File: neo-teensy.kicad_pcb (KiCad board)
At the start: 2 copper layers, 30.5 x 38.1 mm, 32 parts, among them J1 Conn_01x03_Male, J10 Conn_01x14, J11 Conn_02x04_Odd_Even, J12 Conn_01x02, J2 Conn_01x03_Male, J3 Conn_01x14_Male, J4 Conn_01x03_Male, J5 Conn_01x05_Male, J6 Conn_01x03_Male, J7 Conn_01x14_Male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

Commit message: Minor silk-screen fix.
Signed-off-by: Aaron Williams <aaron.w2@gmail.com>
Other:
- board text added: "Neo Teensy"
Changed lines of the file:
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@@
   (general
     (thickness 1.6)
-    (drawings 39)
+    (drawings 40)
     (tracks 545)
     (zones 0)
@@
     )
   )
+  (gr_text "Neo Teensy" (at 35.3949 45.0723 90) (layer B.SilkS)
+    (effects (font (size 1.5 1.5) (thickness 0.15)) (justify mirror))
+  )
   (gr_line (start 27.7368 38.7604) (end 27.7876 38.2016) (layer B.SilkS) (width 0.12))
   (gr_text DO (at 23.7744 67.564 90) (layer F.SilkS)
@@
     (effects (font (size 1 1) (thickness 0.15)) (justify mirror))
   )
-  (gr_text "NeoPixel Driver Board\n© 2019 by Aaron Williams\nDesigned for Teensy 3.2 and 4.0" (at 30.7721 45.847 90) (layer B.SilkS)
+  (gr_text "NeoPixel Driver Board\n© 2019 by Aaron Williams\nDesigned for Teensy 3.2 and 4.0" (at 30.2895 49.022 90) (layer B.SilkS)
     (effects (font (size 1 1) (thickness 0.15)) (justify mirror))
   )

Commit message: Minor cleanup.
Signed-off-by: Aaron Williams <aaron.w2@gmail.com>
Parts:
- moved J10 0.05 mm to (21.6, 67.6)
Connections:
- J10 pad 1: /DO_R -> /DO
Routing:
- net GND: track 139.6 -> 177.2 mm, vias 49 -> 53
- net /DO: track 6.82 -> 34.1 mm
- net /IO0: track 8.57 -> 7.89 mm
- net (no net): vias 1 -> 0

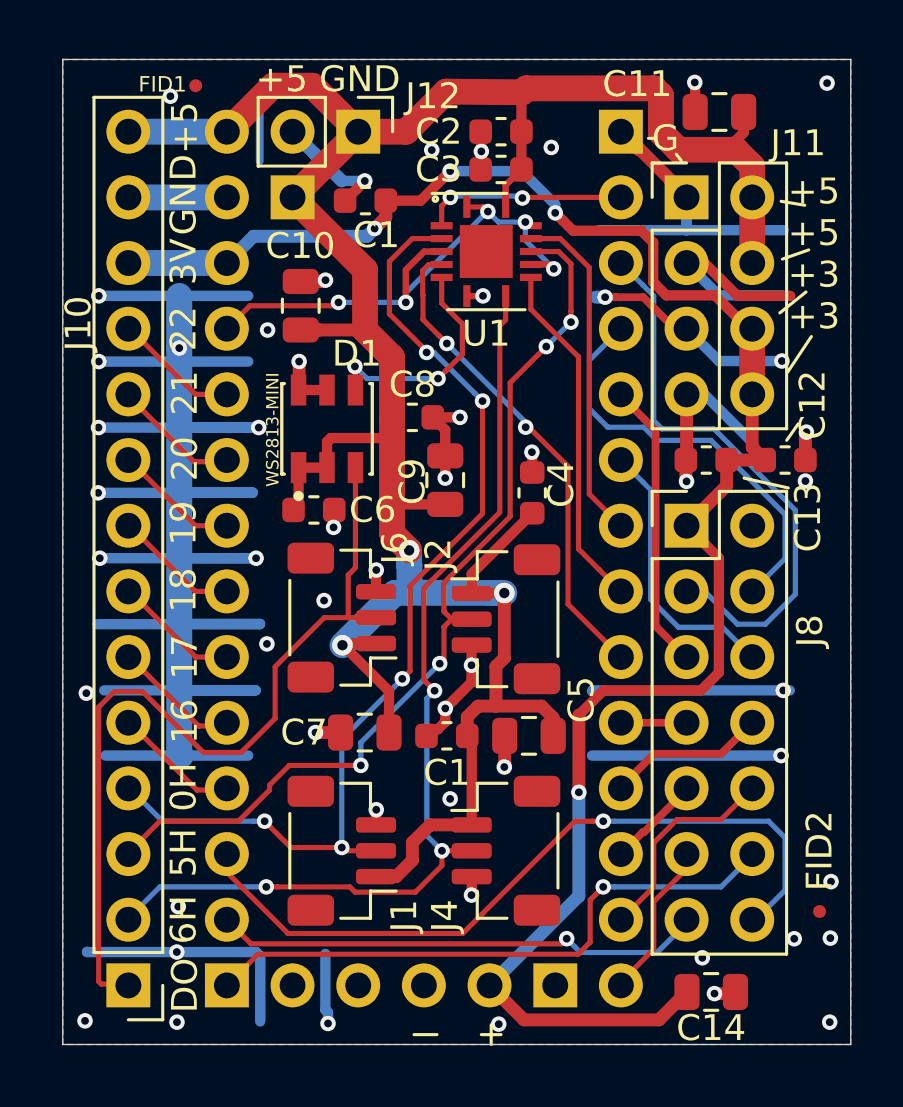
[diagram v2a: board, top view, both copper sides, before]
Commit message: Removed connectors and added 12V boost
Version 3.1.0

Signed-off-by: Aaron Williams <aaron.w2@gmail.com>
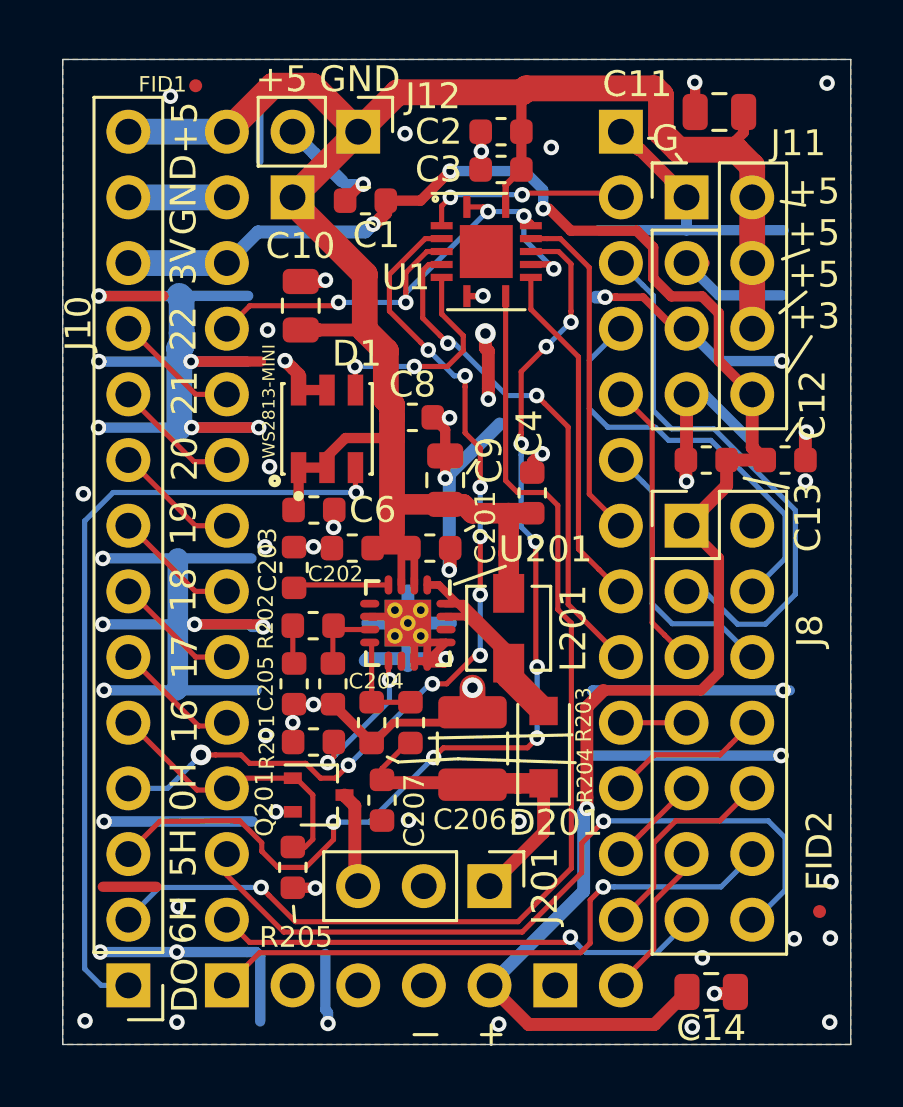
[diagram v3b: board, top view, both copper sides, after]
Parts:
- removed the C1 at (33.9, 57.9)
- removed C5, C7: 10uF, Capacitor_SMD:C_0805_2012Metric
- removed J1, J2, J4, J6: Conn_01x03_Male, Connector_JST:JST_SH_BM03B-SRSS-TB_1x03-1MP_P1.00mm_Vertical
- added C201: 6.8uF, Capacitor_SMD:C_0603_1608Metric, F.Cu at (33.2, 50.6)
- added C202: 100nF, Capacitor_SMD:C_0603_1608Metric, F.Cu at (30.2, 50.6)
- added C203: 22nF, Capacitor_SMD:C_0603_1608Metric, F.Cu at (28.0, 51.4)
- added C204: 820pF, Capacitor_SMD:C_0603_1608Metric, F.Cu at (29.5, 55.9)
- added C205: 47nF, Capacitor_SMD:C_0603_1608Metric, F.Cu at (28.0, 55.9)
- added C206: 22uF, Capacitor_SMD:C_1210_3225Metric, F.Cu at (34.9, 58.4)
- added C207: 1uF, Capacitor_SMD:C_0603_1608Metric, F.Cu at (31.4, 60.4)
- added D201: SS24FL, Diode_SMD:D_SOD-123F, F.Cu at (37.6, 58.4)
- added J201: Conn_01x03, Connector_PinHeader_2.54mm:PinHeader_1x03_P2.54mm_Vertical, F.Cu at (35.6, 63.7)
- added L201: 3.3uH, Aaron:L_Vishay_IHLP-1212, F.Cu at (36.3, 53.8)
- added Q201: BSS214NW, Package_TO_SOT_SMD:SOT-323_SC-70, F.Cu at (28.9, 60.2)
- added R201: 18.2k, Resistor_SMD:R_0603_1608Metric, F.Cu at (28.8, 58.1)
- added R202: 1.69k, Resistor_SMD:R_0603_1608Metric, F.Cu at (28.7, 53.6)
- added R203: 86.6k, Resistor_SMD:R_0603_1608Metric, F.Cu at (32.5, 57.4)
- added R204: 10k, Resistor_SMD:R_0603_1608Metric, F.Cu at (31.0, 57.4)
- added R205: 100k, Resistor_SMD:R_0603_1608Metric, F.Cu at (27.9, 63.0)
- added U201: TPS55340-Q1, Aaron:QFN-16-1EP_3x3mm_P0.5mm_EP2.7x2.7mm_ThermalVias, F.Cu at (32.4, 53.5)
- moved REF** 2.78 mm to (36.1, 56.2)
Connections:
- net /IO16 renamed FET_CTL
- J11 pad 6: +3V3 -> +5V
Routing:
- net +5V: track 106.6 -> 82.4 mm, vias 3 -> 0
- net /12-Boost/SW: track 0.00 -> 13.8 mm
- net +12V: track 0.00 -> 13.1 mm
- net GND: track 177.2 -> 186.7 mm, vias 53 -> 64
- net FET_CTL: track 4.94 -> 11.3 mm
- net /12-Boost/FREQ: track 0.00 -> 5.83 mm, vias 0 -> 2
- net /IO5_H: track 36.0 -> 41.0 mm, vias 4 -> 8
- net /IO6_H: track 38.2 -> 42.8 mm, vias 3 -> 1
- net /IO0_H: track 39.6 -> 35.5 mm, vias 5 -> 9
- net /12-Boost/FB: track 0.00 -> 3.84 mm
- net /12-Boost/FET_DRV: track 0.00 -> 3.74 mm
- net /12-Boost/SS: track 0.00 -> 3.70 mm
- net /12-Boost/COMP: track 0.00 -> 2.93 mm
- net /DO: track 34.1 -> 31.2 mm, vias 0 -> 1
- net Net-(C205-Pad1): track 0.00 -> 1.48 mm
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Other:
- board text added: "+5 +5 +5 +3"
- board text added: "Revision 3.1"
- board text removed: "+5 +5 +3 +3"
- board text removed: "Revision 3.0"

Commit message: Fixed GPIO 13, GPIO 16 and GPIO 17 for the fan control.
Signed-off-by: Aaron Williams <aaron.w2@gmail.com>
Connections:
- J10 pad 5: FET_CTL -> /IO13
- J10 pad 6: /IO17 -> FET_CTL
- J7 pad 4: FET_CTL -> /IO16
- J7 pad 5: /IO17 -> FET_CTL
- J8 pad 12: /IO13 -> /IO14
- J8 pad 13: /IO14 -> /IO15
- J8 pad 14: /IO15 -> /IO16
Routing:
- net GND: track 186.7 -> 245.8 mm, vias 64 -> 69
- net /IO16: track 0.00 -> 32.0 mm, vias 0 -> 1
- net /IO15: track 29.9 -> 20.6 mm, vias 1 -> 0
- net /IO13: track 23.5 -> 14.8 mm, vias 1 -> 0
- net /IO17: track 4.81 -> 0.00 mm
- net /IO14: track 19.0 -> 23.4 mm, vias 1 -> 0
- net /IO20: track 4.91 -> 6.07 mm
- net FET_CTL: track 11.3 -> 12.3 mm
- net /IO6_H: track 42.8 -> 42.6 mm, vias 1 -> 2
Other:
- rule trace_min: 0.2 -> 0.1524
- rule via_min_drill: 0.3 -> 0.254
- rule via_min_size: 0.4 -> 0.508
- board text added: "13"
- board text added: "GND +5"
- board text added: "Revision 3.1.1"
- board text removed: "+5 GND"
- board text removed: "16"
- board text removed: "Revision 3.1"

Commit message: Minor fixups, changed solder mask.
Signed-off-by: Aaron Williams <aaron.w2@gmail.com>
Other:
- rule pad_to_mask_clearance: 0.051 -> 0.0508
- rule solder_mask_min_width: 0.25 -> 0.101
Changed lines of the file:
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@@
   )
   (setup
-    (last_trace_width 0.8)
+    (last_trace_width 0.25)
     (user_trace_width 0.1524)
     (user_trace_width 0.2)
@@
     (pad_size 1.7 1.7)
     (pad_drill 1)
-    (pad_to_mask_clearance 0.051)
-    (solder_mask_min_width 0.25)
+    (pad_to_mask_clearance 0.0508)
+    (solder_mask_min_width 0.101)
     (aux_axis_origin 0 0)
     (visible_elements FFFFFF7F)

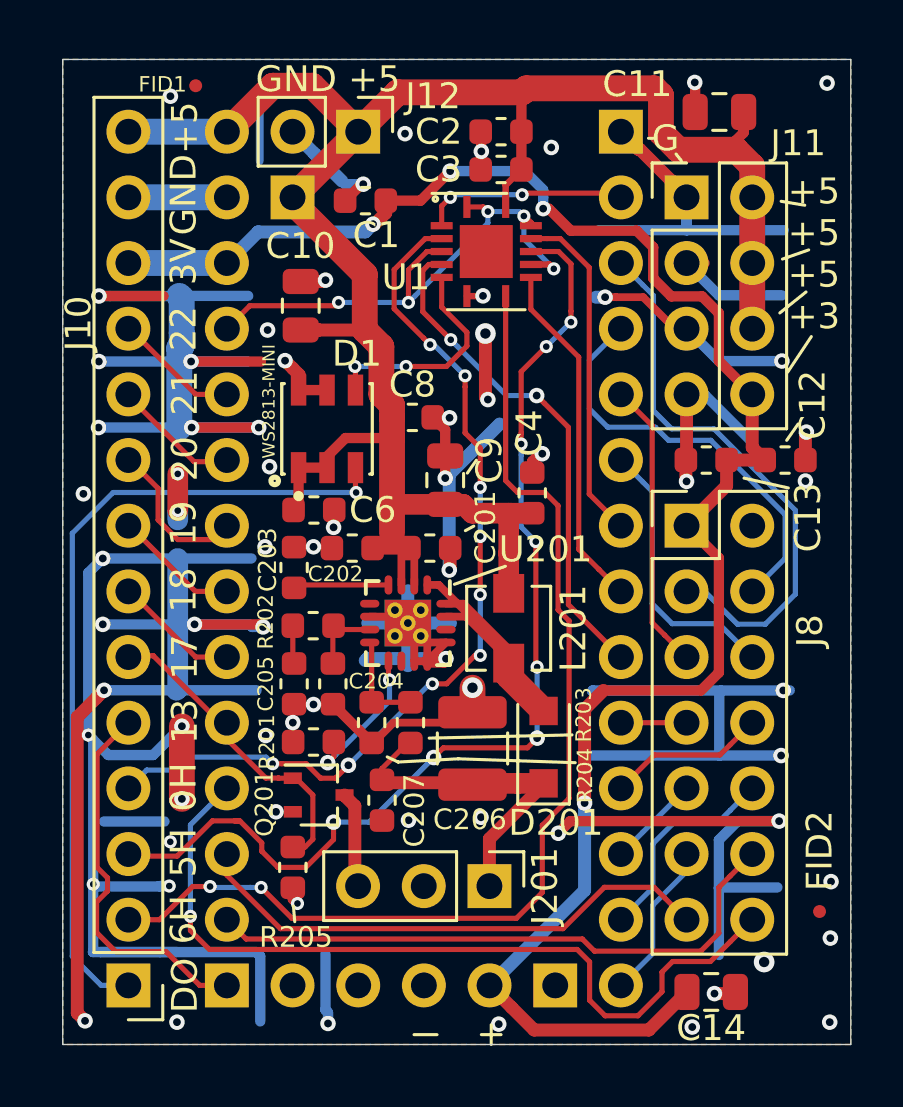
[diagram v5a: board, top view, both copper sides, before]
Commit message: Changed GPIOs for Teensy 4.0
The 5V GPIOs were changed for the Teensy 4.0.  In addition the GPIOs to
the 14 pin header were also changed.

Some component values were also changed for the power supply.

Note that this is still compatible with the 3.1 stencil.

This also fixes the 12V BOM.

Signed-off-by: Aaron Williams <aaron.w2@gmail.com>
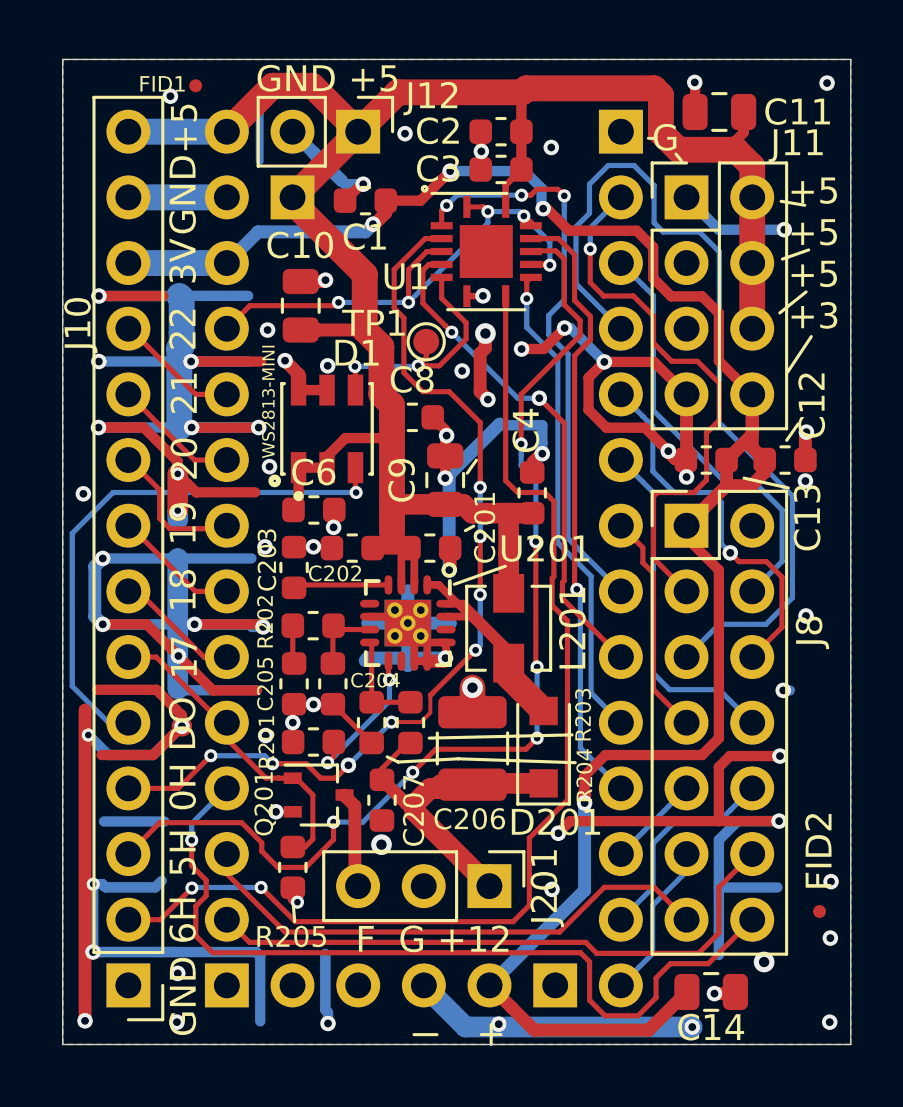
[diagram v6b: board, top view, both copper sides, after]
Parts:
- added TP1: TestPoint, TestPoint:TestPoint_Pad_D1.0mm, F.Cu at (33.1, 42.7)
- C201: value 6.8uF -> 22uF
- C202: value 100nF -> 0.1uF
- C206: value 22uF -> 47uF
- C6: value 0.1uF -> 1uF
- R201: value 18.2k -> 18.7K
- R202: value 1.69k -> 1.62k
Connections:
- net /IO5_H renamed /IO9_H
- J10 pad 1: /DO -> GND
- J10 pad 2: /IO6_H -> /IO8_H
- J10 pad 4: /IO0_H -> /IO6_H
- J10 pad 5: /IO13 -> /DO
- J8 pad 3: /IO1 -> /IO0
- J8 pad 4: /IO2 -> /IO1
- J8 pad 5: /IO3 -> /IO2
- J8 pad 6: /IO4 -> /IO3
- J8 pad 7: /IO8 -> /IO5
- J8 pad 8: /IO9 -> /IO4
- U1 pad 12: /IO5 -> /IO9
- U1 pad 2: /IO0 -> /IO6
- U1 pad 3: /IO0_H -> /IO6_H
- U1 pad 8: /IO6_H -> /IO8_H
- U1 pad 9: /IO6 -> /IO8
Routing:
- net /IO8_H: track 0.00 -> 42.7 mm, vias 0 -> 2
- net /IO0_H: track 35.1 -> 0.00 mm, vias 9 -> 0
- net /IO9: track 6.13 -> 23.8 mm, vias 0 -> 1
- net /IO2: track 16.4 -> 33.7 mm
- net /IO8: track 2.54 -> 18.8 mm, vias 0 -> 1
- net /IO13: track 14.8 -> 0.00 mm
- net /IO0: track 7.97 -> 21.5 mm, vias 2 -> 1
- net /DO: track 31.6 -> 21.3 mm
- net GND: track 245.8 -> 236.6 mm, vias 69 -> 74
- net /IO6: track 13.6 -> 22.5 mm, vias 0 -> 3
- net /IO6_H: track 42.6 -> 35.9 mm, vias 2 -> 8
- net /IO1: track 21.8 -> 16.4 mm
- net /IO5: track 13.2 -> 8.67 mm
- net +3V3: track 72.2 -> 75.8 mm
- net /IO3: track 11.2 -> 14.7 mm, vias 0 -> 1
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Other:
- board text added: "F G +12"
- board text added: "NeoPixel Driver Board © 2019 by Aaron Williams Designed for Teensy 4.0 and 3.2"
- board text added: "Revision 3.2.0"
- board text added: "U201:"
- board text removed: "13"
- board text removed: "NeoPixel Driver Board © 2019 by Aaron Williams Designed for Teensy 3.2 and 4.0"
- board text removed: "Revision 3.1.1"

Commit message: Added pull-up resistors to 14-pin header
Made board 4 layers

Made board double sided

Signed-off-by: Aaron Williams <aaron.w2@gmail.com>
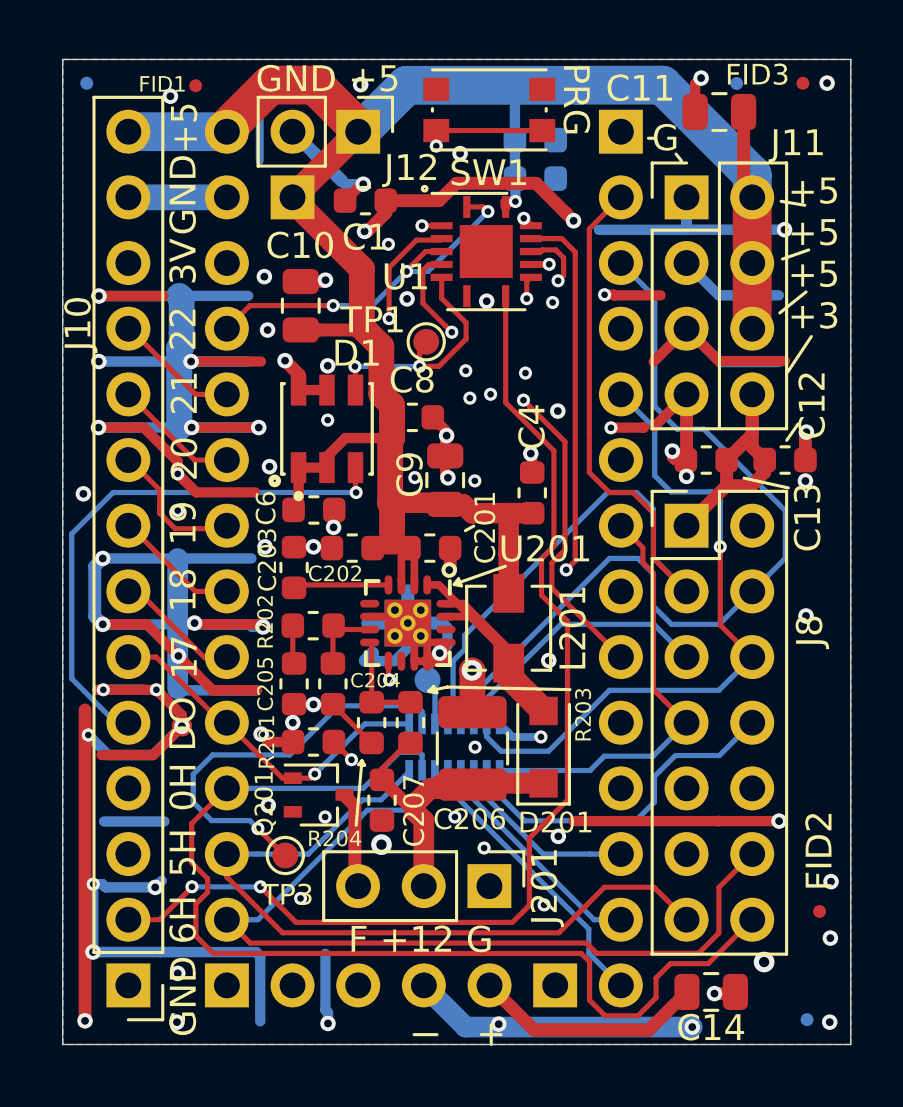
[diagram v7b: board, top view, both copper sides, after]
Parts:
- removed R205: 100k, Resistor_SMD:R_0603_1608Metric
- removed REF**: KiCad-Logo2_5mm_SilkScreen, Symbol:KiCad-Logo2_5mm_SilkScreen
- added FID3: FIDUCIAL_1MM, Fiducial:Fiducial_0.5mm_Mask1mm, F.Cu at (47.7, 32.7)
- added FID4: FIDUCIAL_1MM, Fiducial:Fiducial_0.5mm_Mask1mm, B.Cu at (20.0, 32.7)
- added FID5: FIDUCIAL_1MM, Fiducial:Fiducial_0.5mm_Mask1mm, B.Cu at (45.1, 32.7)
- added FID6: FIDUCIAL_1MM, Fiducial:Fiducial_0.5mm_Mask1mm, B.Cu at (47.8, 68.9)
- added RN1: 100K, Resistor_SMD:R_Array_Convex_8x0602, B.Cu at (34.2, 58.4)
- added SW1: SW_SPST_KMR2, Aaron:SW_SPST_KMR2, F.Cu at (35.5, 33.7)
- added TP2: TestPoint, TestPoint:TestPoint_Pad_D1.0mm, B.Cu at (33.2, 55.8)
- added TP3: TestPoint, TestPoint:TestPoint_Pad_D1.0mm, F.Cu at (27.7, 62.5)
- C2, C3: moved to B.Cu
- moved C3 1.37 mm to (37.3, 36.4), turned to 0 degrees
- moved C2 1.37 mm to (37.3, 34.9), turned to 0 degrees
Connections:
- J201 pad 1: +12V -> GND
- J201 pad 2: GND -> +12V
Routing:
- net /Program: track 0.00 -> 41.5 mm, vias 0 -> 2
- net /IO1: track 16.4 -> 33.1 mm
- net Net-(RN1-Pad10): track 0.00 -> 16.0 mm, vias 0 -> 1
- net /IO4: track 13.4 -> 29.2 mm
- net GND: track 236.6 -> 251.0 mm, vias 74 -> 85
- net /IO0: track 21.5 -> 35.6 mm, vias 1 -> 0
- net +3V3: track 75.8 -> 87.2 mm, vias 4 -> 3
- net /IO12: track 6.13 -> 17.2 mm
- net /IO3: track 14.7 -> 25.7 mm
- net /IO14: track 23.5 -> 34.2 mm
- net /IO11: track 8.18 -> 17.1 mm
- net /IO16: track 32.3 -> 41.1 mm, vias 1 -> 0
- net /IO15: track 20.7 -> 29.2 mm
- net /IO6_H: track 35.9 -> 27.9 mm, vias 8 -> 1
- net /IO5: track 8.67 -> 16.7 mm
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- added copper zone on In1.Cu, net GND
- added copper zone on In2.Cu, net GND
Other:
- copper layers 2 -> 4
- board text added: "F +12 G"
- board text added: "NeoPixel Driver Board © 2020 by Aaron Williams Designed for Teensy 4.0 and 3.2"
- board text added: "PRG"
- board text added: "Revision 3.3.0"
- board text removed: "F G +12"
- board text removed: "NeoPixel Driver Board © 2019 by Aaron Williams Designed for Teensy 4.0 and 3.2"
- board text removed: "Revision 3.2.0"
